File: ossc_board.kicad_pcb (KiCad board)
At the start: 2 copper layers, 91.2 x 167 mm, 340 parts, among them J1 HDMI_CONN (10029449-111RLF), J10 COLOR INPUT, J11 MONO INPUT, J12 NEXT PWR INPUT 1, J13 NEXT PWR INPUT 2, J14 -12VDC OUT, J15 5VDC STANDBY, J16 MON IN 1, J17 MON IN 2, J18 PA1, J19 BOOT0, J2 OUT (SJ1-3535NG), J20 PC0, J21 PC1, J22 PB0, J23 PB1, J24 R SPK, J25 R SPEAKER (SJ-2509N), J26 L SPEAKER, J27 L SPK, J28 I2C Ext, J29 OLED, J3 MIC (SJ1-3535NG), J30 BOOT1, J31 NeXT Keyboard, J32 NeXT Keyboard (MD-50SM / KMDG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, J4 USB Host (SS-52100-001), J5 Mic IN, J6 Audio OUT, J7 STLINK, J8 UART2, J9 PA0, P1 JTAG (30310-6002HB), Q1 2SC2712, SW1 NeXT POWER SW (1-1825027-1 / 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, SW2 BTN0, SW3 NeXT POWER SW, SW4 MCU RESET, U1 TVP7002PZP, U10 S25FL216K (IS25LP016D-JBLE), U11 TLV70033DDCR, U12 TLV70012DDCT, U13 TLV70025DDCT, U14 TLV70012DDCT, U15 TLV70018DDCT, U16 TLV70018DDCT, U17 USBLC6-2SC6, U18 STMPS2151STR‎ or TPS2051CDBV, U19 SN74LVC2G34DBV, U2 EP4CE15E22C8N, U20 PCM5122PW, U21 TLV70033DDCR (or XC6204B332MR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, U22 TLV70033DDCR (or XC6204B332MR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, U23 PLT133/T, U24 STM32F401RCT6, U25 SN74LVC1G07DBV, U26 SN74HCT125DR, U27 TLV320ADC3100, U28 BD33FC0FP, U29 TPA2005D1DGN, U3 IT6613E, U30 BD33FC0FP, U31 TPA2005D1DGN, U32 PCA9515AD, U4 SN74LVC2G17DBV, U5 BD33FC0FP, U6 TLV70033DDCR, U7 NCP703SN19T1G, U8 5V(DC/DC), U9 TLV70019DDCT, X1 ACHL-27MHZ-EK, X2 ASEDV-27.000MHZ-LR-T(ECS-2333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, X3 ECS-2520MVLC-225.792-BN-TR, Y2 25MHz (FA-238 25.0000MB-K0)

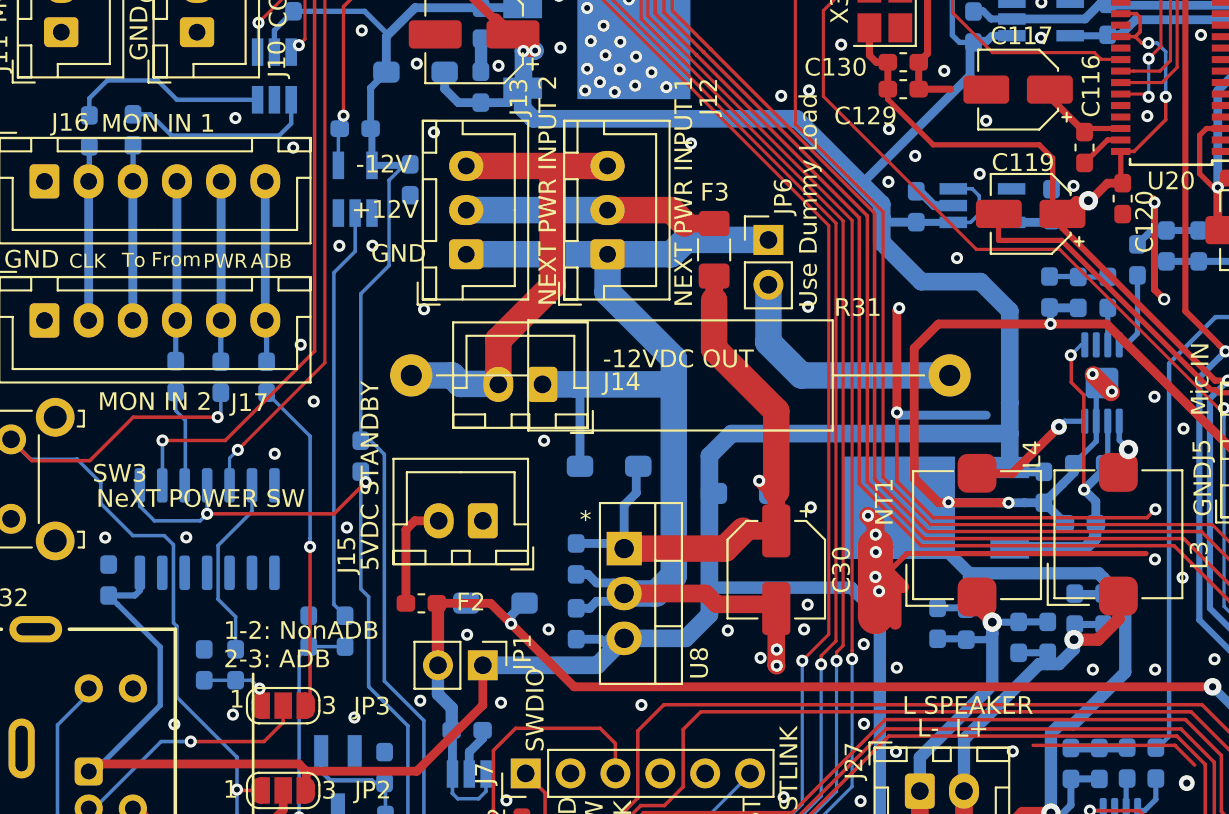
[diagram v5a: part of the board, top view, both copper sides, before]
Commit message: connect XSMT (errata)
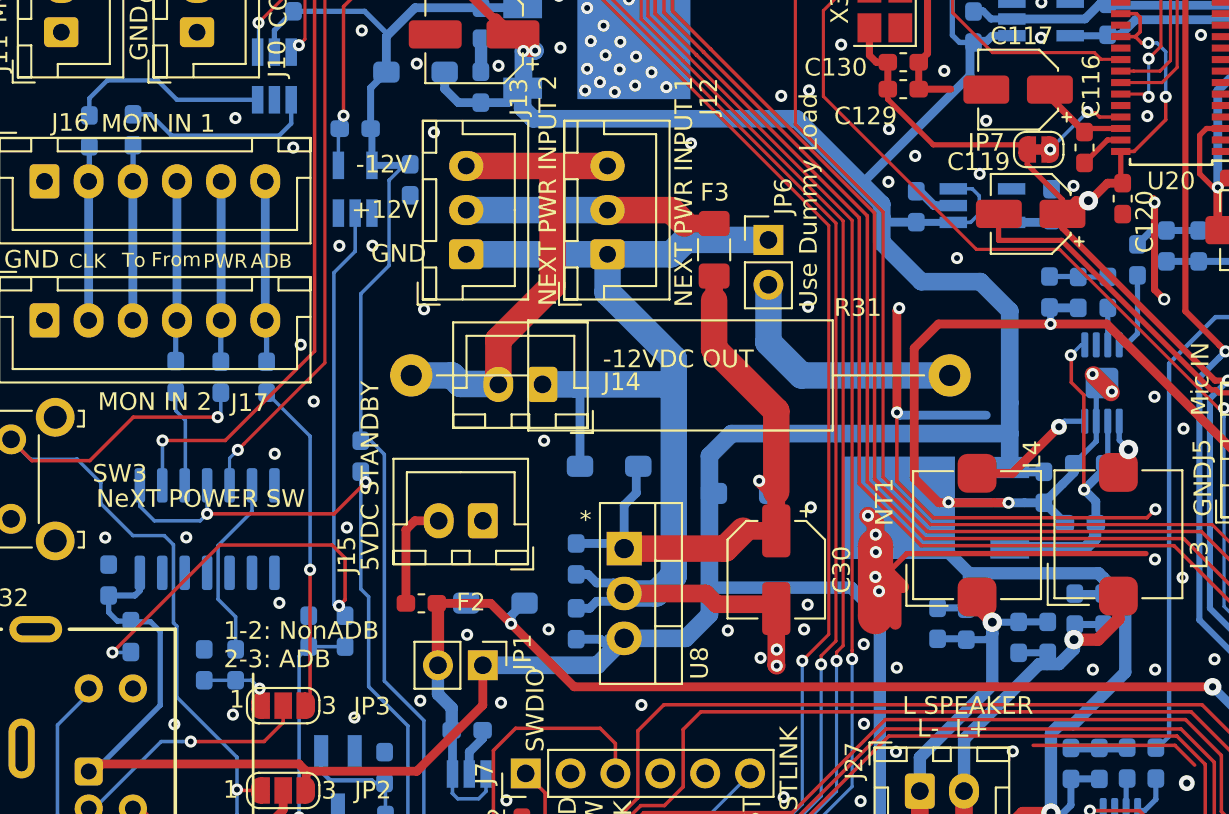
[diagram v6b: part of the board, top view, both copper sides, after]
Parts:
- added JP7: JMP XSMT, Jumper:SolderJumper-2_P1.3mm_Bridged_RoundedPad1.0x1.5mm, F.Cu at (98.6, 106.6)
- added R53: (100k), Resistor_SMD:R_0603_1608Metric_Pad1.05x0.95mm_HandSolder, B.Cu at (47.2, 134.2)
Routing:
- net Net-(R29-Pad1): track 23.6 -> 43.5 mm, vias 0 -> 2
- net Net-(JP7-Pad2): track 0.00 -> 5.00 mm, vias 0 -> 2
- net /hdmitx1/5V: track 308.4 -> 309.6 mm
- net /soundbox/A_DVDD: track 86.0 -> 85.4 mm
- net GND: vias 371 -> 372

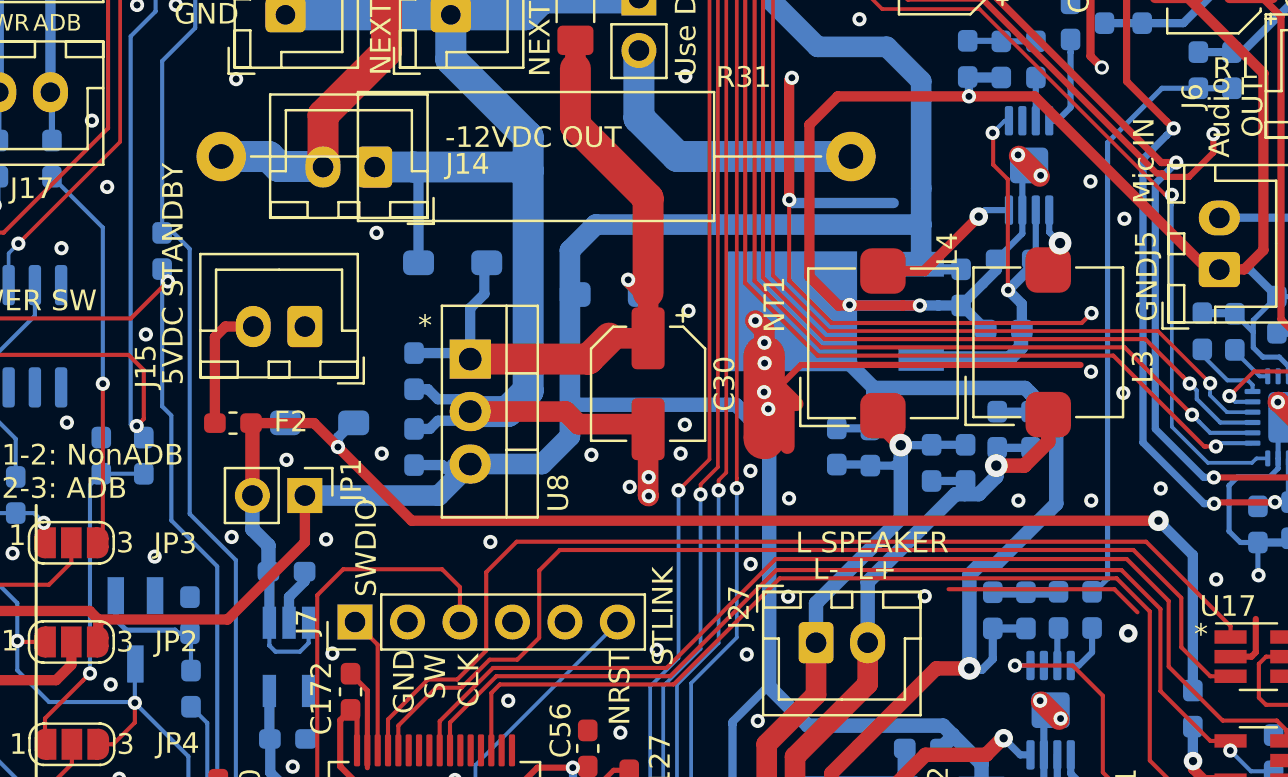
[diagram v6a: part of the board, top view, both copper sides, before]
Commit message: add protection zener
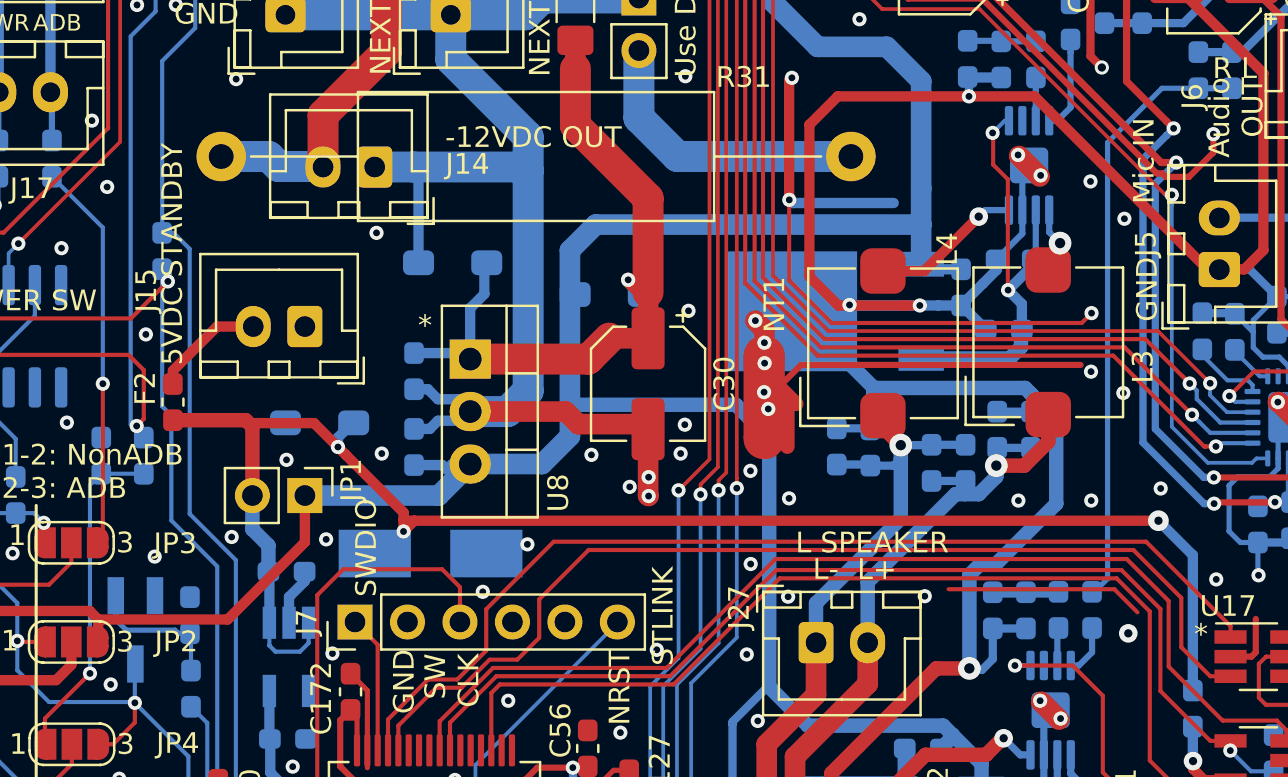
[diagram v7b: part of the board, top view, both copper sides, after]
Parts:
- added D10: ZD 5.6V (1SMB5919BT3G), Diode_SMD:D_SMB_Handsoldering, B.Cu at (73.2, 138.6)
- moved F2 3.08 mm to (60.7, 131.3), turned to 270 degrees
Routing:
- net /soundbox/5VDC_STBY: track 70.7 -> 76.0 mm, vias 2 -> 3
- net Net-(U17-Pad1): track 50.3 -> 49.2 mm
- net Net-(U17-Pad3): track 50.8 -> 50.0 mm
- net Net-(F2-Pad1): track 6.23 -> 5.42 mm
- net GND: vias 372 -> 373
